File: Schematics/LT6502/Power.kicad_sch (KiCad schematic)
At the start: 87 parts, among them IC2 MP2636GR-P, J2 USBPD_PROG, J3 USB_C_Receptacle_USB2.0_16P, J4 BATTERY JST PH-2A, Q1 STL9P3LLH6, Q3 STL9P3LLH6, U6 STUSB4500QTR, U7 AP63203WU

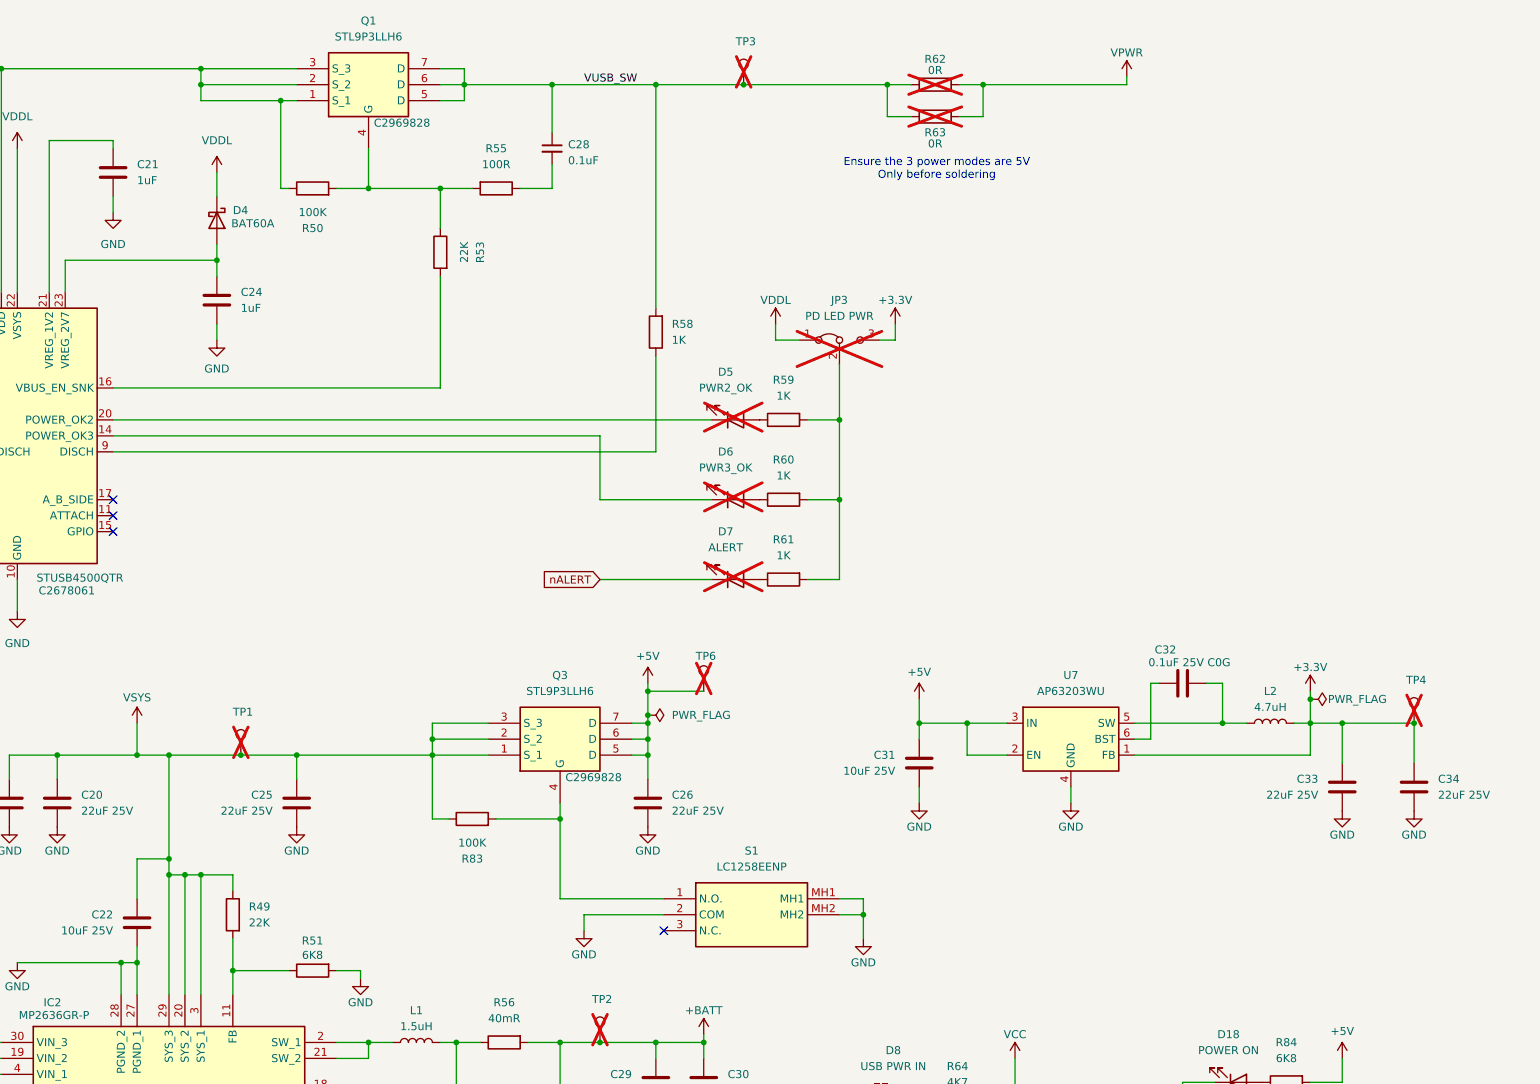
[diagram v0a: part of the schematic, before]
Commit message: Updated Schematics
Added bulk capacitance with higher ESR to help with display PLL starting
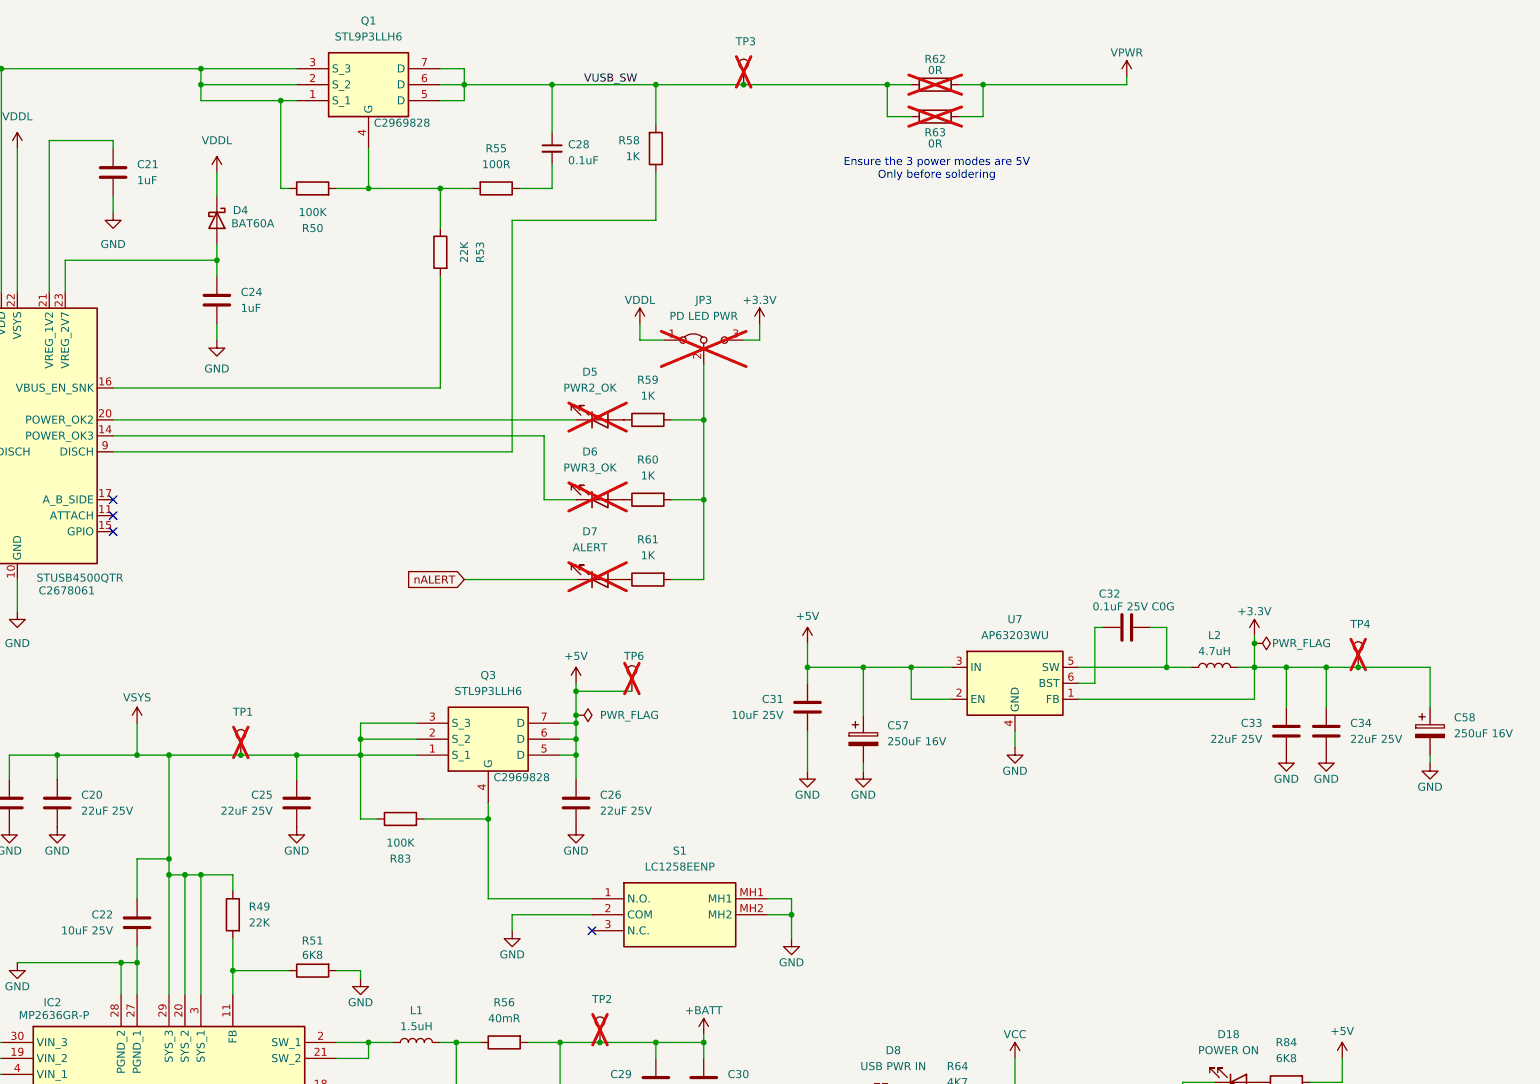
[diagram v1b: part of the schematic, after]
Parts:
- added C57, C58: 250uF 16V, Capacitor_SMD:CP_Elec_10x12.5, symbol Device:C_Polarized
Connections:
- net +3.3V: now also C58.1
- net +5V: now also C57.1
- net GND: now also C57.2, C58.2
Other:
- moved on the sheet: C26, C31, C32, C33, C34, D5, D6, D7, JP3, L2, Q3, R58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

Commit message: Updated current limits
Updated the current limits as we were pushing the previous limit (900mA) with display, keyboard and CF
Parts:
- R46: value 51K -> 24K
- R48: value 42K2 -> 33K; LCSC C11565 -> (none)
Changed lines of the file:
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@@
 		)
 	)
-	(text_box "Rilim = 15K\ngives max charge current 3A!\n\nRilim = 51K\ngives max charge of 900mA\n\n"
+	(text_box "Input TOTAL Max current is;\nRilim = 15K -> Gives max 3A\nRilim = 24K -> gives max 1.75A\nRilim = 51K -> gives max 900mA\n\n"
 		(exclude_from_sim no)
-		(at 114.3 226.06 0)
-		(size 31.75 16.51)
+		(at 109.22 226.06 0)
+		(size 36.83 16.51)
 		(margins 0.9525 0.9525 0.9525 0.9525)
 		(stroke
@@
 	(text_box "Riset = 62K \nRsense = 40mR\ngives 960mA charging\n\nRiset = 120K\nRSense = 40mR\nGives 500mA charging"
 		(exclude_from_sim no)
-		(at 114.3 245.11 0)
-		(size 31.75 16.51)
+		(at 109.22 245.11 0)
+		(size 36.83 16.51)
 		(margins 0.9525 0.9525 0.9525 0.9525)
 		(stroke
@@
 		)
 	)
-	(text_box "Rolim = 42.2K\ngives sax output current 1.3A\n\nRolim = 22K\nGives max output current 2.5A"
+	(text_box "Max current from battery is;\nRolim = 42.2K -> Gives 1.3A\nRolim = 33K   -> Gives 1.67A\nRolim = 22K   -> Gives 2.5A\n"
 		(exclude_from_sim no)
-		(at 114.3 264.16 0)
-		(size 31.75 16.51)
+		(at 109.22 265.43 0)
+		(size 36.83 11.43)
 		(margins 0.9525 0.9525 0.9525 0.9525)
 		(stroke
@@
 			)
 		)
-		(property "Value" "51K"
+		(property "Value" "24K"
 			(at 159.9988 233.5961 90)
 			(effects
@@
 			)
 		)
-		(property "Value" "42K2"
+		(property "Value" "33K"
 			(at 176.5088 243.7561 90)
 			(effects
@@
 			)
 		)
-		(property "LCSC" "C11565"
+		(property "LCSC" ""
 			(at 176.53 241.3 90)
 			(effects
